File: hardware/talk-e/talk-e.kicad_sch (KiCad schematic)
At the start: 1 part, among them U1 RFM96W-433S2

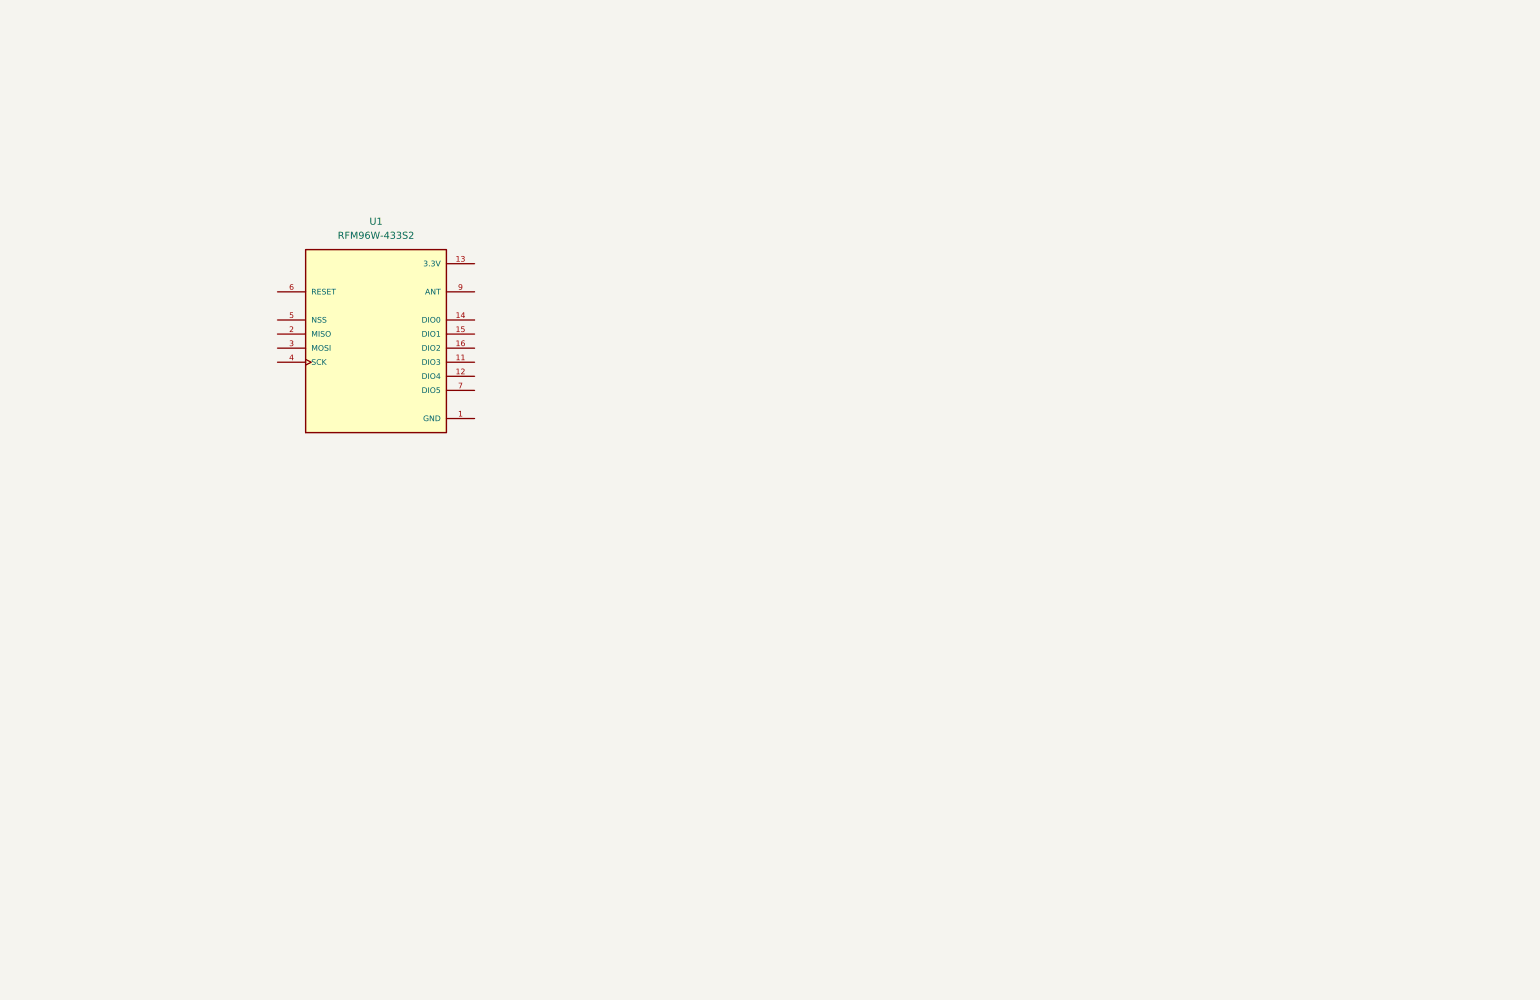
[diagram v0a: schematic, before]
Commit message: Progress on battery charging schematic
TP4056 + DW01A + FS8205A
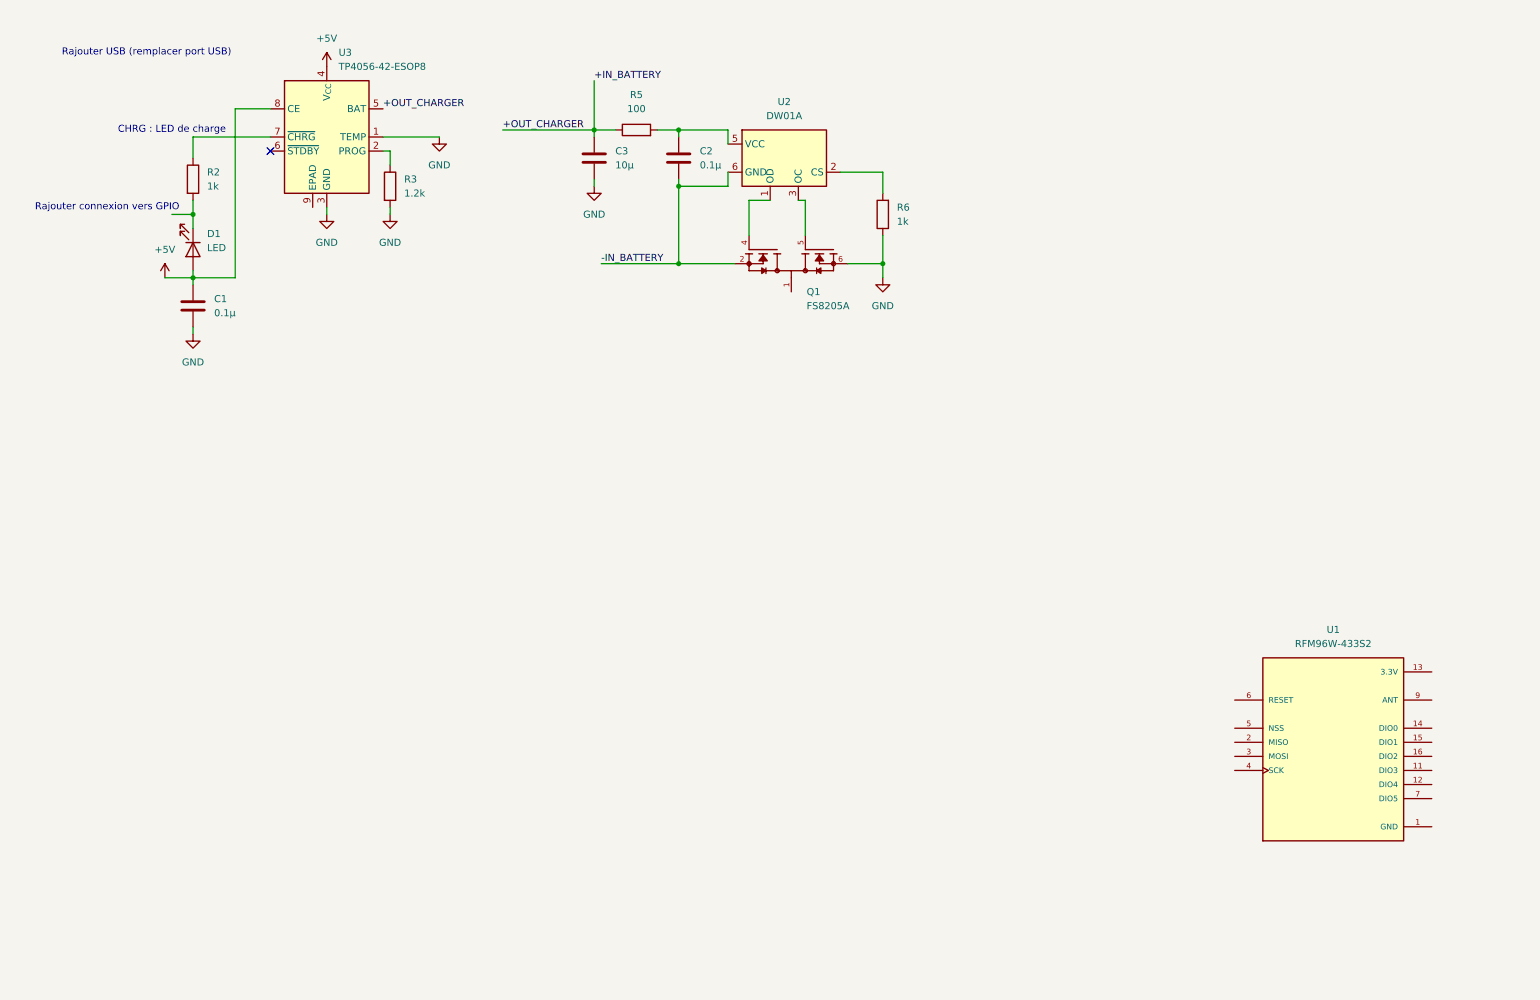
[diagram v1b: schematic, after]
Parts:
- added C1, C2: 0.1µ, symbol Device:C
- added C3: 10µ, symbol Device:C
- added D1: LED, LED_THT:LED_D3.0mm, symbol Device:LED
- added Q1: FS8205A, FS8205A:SOP65P640X120-8N, symbol FS8205A:FS8205A
- added R2, R6: 1k, symbol Device:R
- added R3: 1.2k, symbol Device:R
- added R5: 100, symbol Device:R
- added U2: DW01A, Package_TO_SOT_SMD:SOT-23-6, symbol Battery_Management:DW01A
- added U3: TP4056-42-ESOP8, Package_SO:SOIC-8-1EP_3.9x4.9mm_P1.27mm_EP2.41x3.3mm, symbol Battery_Management:TP4056-42-ESOP8
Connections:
- net GND: now also C1.2, C3.2, Q1.6, Q1.7, R3.2, R6.1, U3.1 (TEMP), U3.3 (GND)
- new net: D1.1 (K), R2.2
- new net: C2.1, R5.2, U2.5 (VCC)
- new net: R6.2, U2.2 (CS)
- new net: R3.1, U3.2 (PROG)
- new net: R2.1, U3.7 (~{CHRG})
- new net: Q1.4, U2.1 (OD)
- new net: Q1.5, U2.3 (OC)
- new net: Q1.1, Q1.8
- new net +5V: C1.1, D1.2 (A), U3.4 (V_{CC}), U3.8 (CE)
- new net +IN_BATTERY: C3.1, R5.1, U3.5 (BAT)
- new net -IN_BATTERY: C2.2, Q1.2, Q1.3, U2.6 (GND)
- no-connect marks 0 -> 1
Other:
- note added: "CHRG : LED de charge"
- note added: "Rajouter USB (remplacer port USB)"
- note added: "Rajouter connexion vers GPIO"
- moved on the sheet: U1

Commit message: Added SX1278 connections to ESP32-S3 in schematic
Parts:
- added U4: ESP32-S3, Package_DFN_QFN:QFN-56-1EP_7x7mm_P0.4mm_EP4x4mm, symbol MCU_Espressif:ESP32-S3
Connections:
- net GND: now also U4.57 (GND)
- net +3.3V: now reaches U1.13 (3.3V)
- net LORA_DIO0: now reaches U1.14 (DIO0)
- net LORA_DIO0: now also U4.14 (GPIO9)
- net LORA_MISO: now reaches U1.2 (MISO)
- net LORA_MISO: now also U4.18 (GPIO13)
- net LORA_MOSI: now reaches U1.3 (MOSI)
- net LORA_MOSI: now also U4.16 (GPIO11)
- net LORA_SCK: now reaches U1.4 (SCK)
- net LORA_SCK: now also U4.17 (GPIO12)
- net LORA_CS: now reaches U1.5 (NSS)
- net LORA_CS: now also U4.15 (GPIO10)
- net LORA_RST: now reaches U1.6 (RESET)
- net LORA_RST: now also U4.13 (GPIO8)
- net ANTENNA: now reaches U1.9 (ANT)
- new net: U4.2 (VDD3P3), U4.3 (VDD3P3)
- new net: U4.55 (VDDA), U4.56 (VDDA)
- no-connect marks 1 -> 6
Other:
- note added: "3.7 V nominal"
- note added: "Brancher la batterie sur IN_BATTERY"
- moved on the sheet: U1

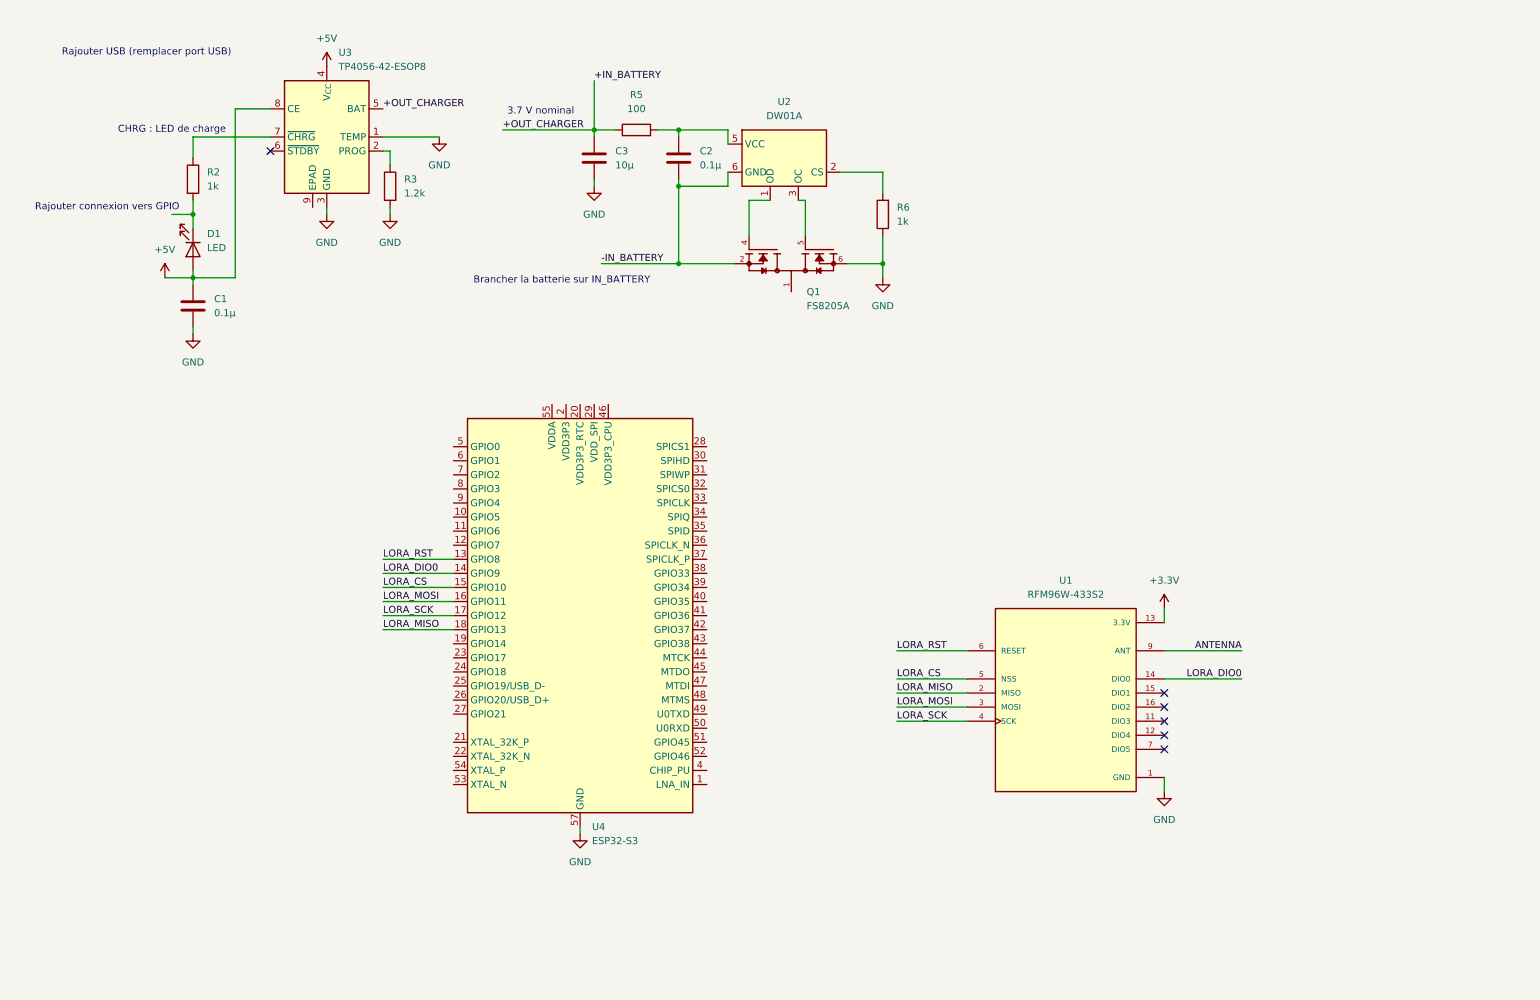
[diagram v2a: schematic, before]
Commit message: Added SH1106 OLED screen to schematic
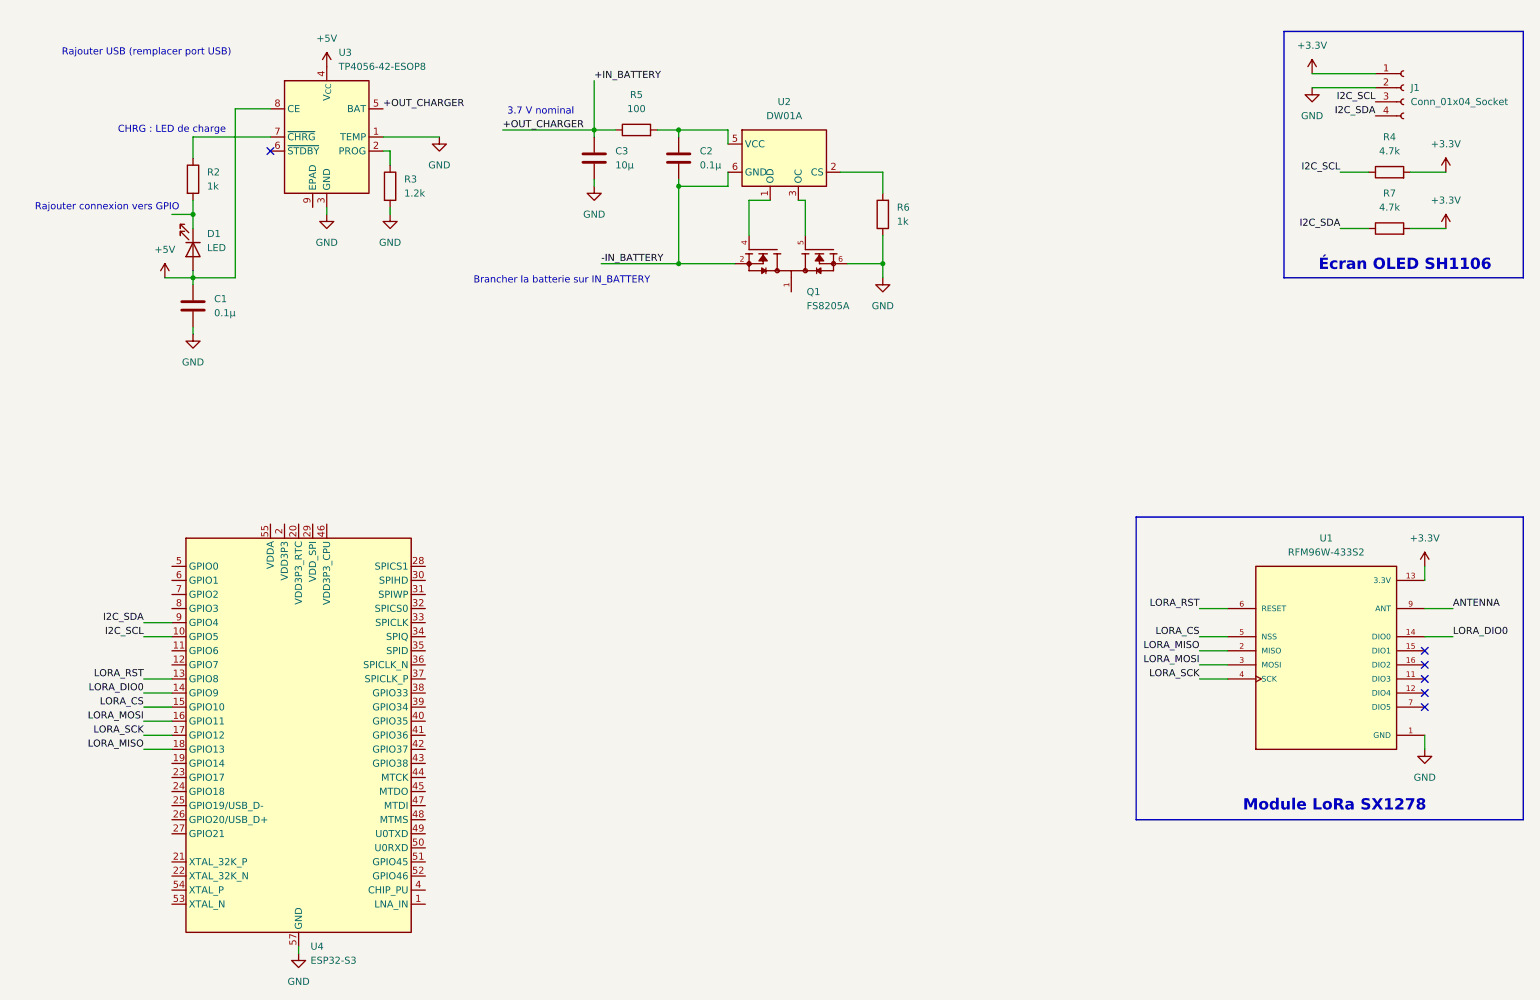
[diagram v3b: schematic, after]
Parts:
- added J1: Conn_01x04_Socket, Connector_PinSocket_2.54mm:PinSocket_1x04_P2.54mm_Vertical, symbol Connector:Conn_01x04_Socket
- added R4, R7: 4.7k, symbol Device:R
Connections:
- net +3.3V: now also J1.1 (Pin_1), R4.2, R7.2
- net GND: now also J1.2 (Pin_2)
- net I2C_SCL: now reaches U4.10 (GPIO5)
- net I2C_SCL: now also J1.3 (Pin_3), R4.1
- net I2C_SDA: now reaches U4.9 (GPIO4)
- net I2C_SDA: now also J1.4 (Pin_4), R7.1
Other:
- note added: "Module LoRa SX1278"
- note added: "Écran OLED SH1106"
- moved on the sheet: U1, U4

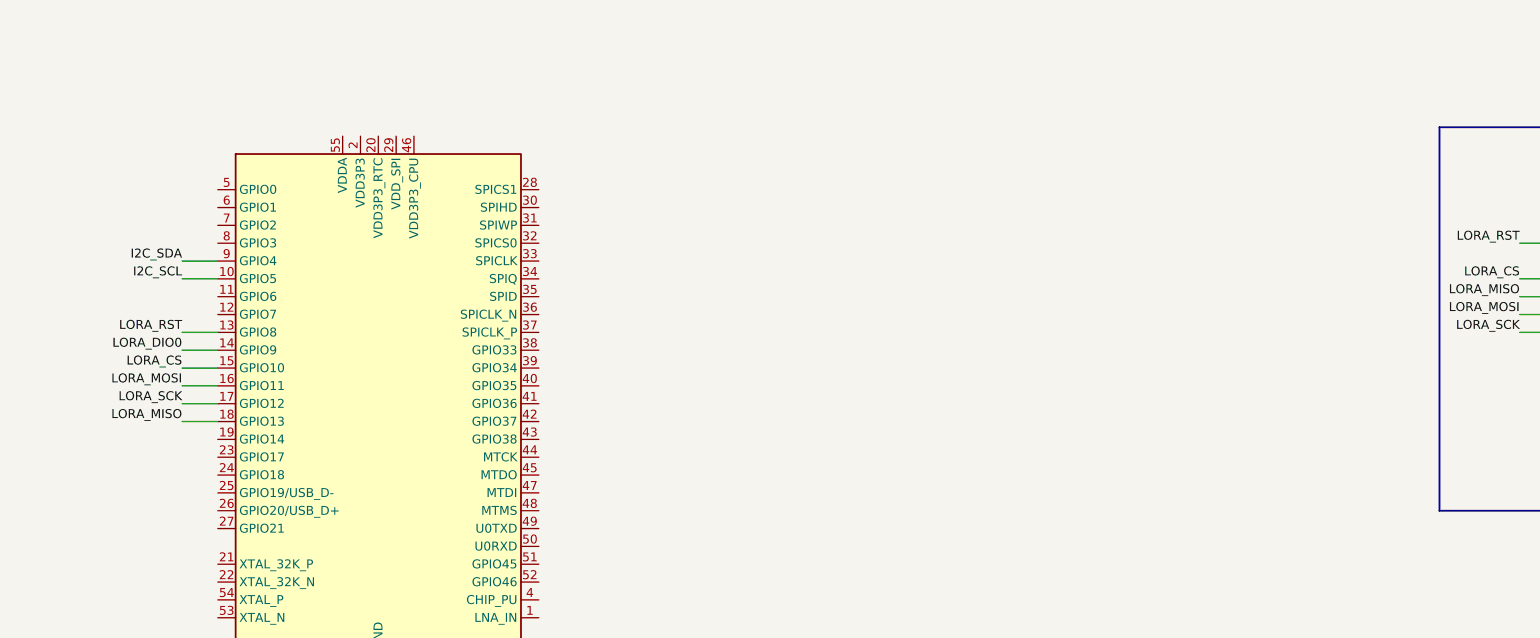
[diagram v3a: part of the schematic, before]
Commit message: Added EC12 incremental encoder to schematic
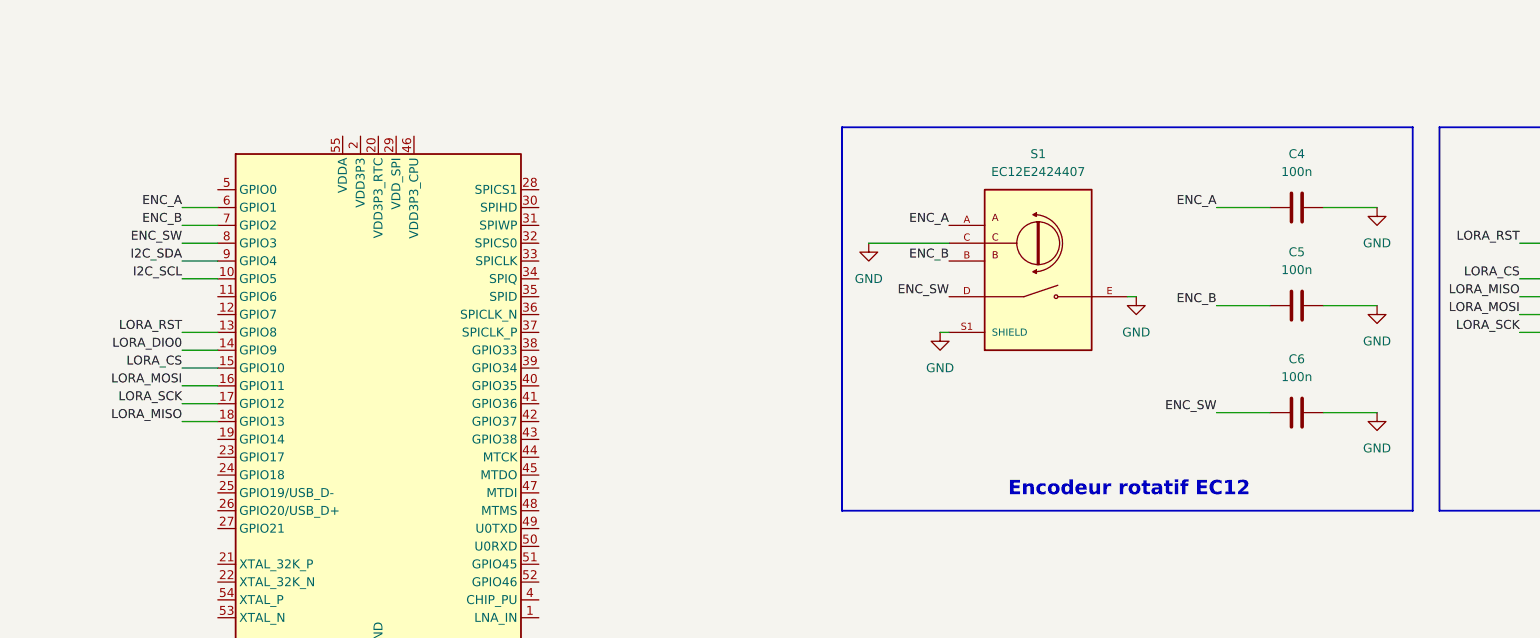
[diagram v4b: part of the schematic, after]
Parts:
- added C4, C5, C6: 100n, symbol Device:C
- added S1: EC12E2424407, EC12E2424407:ALPS_EC12E2424407, symbol EC12E2424407:EC12E2424407
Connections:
- net GND: now also C4.2, C5.2, C6.2, S1.C, S1.E, S1.S1 (SHIELD), S1.S2 (SHIELD)
- net ENC_A: now reaches U4.6 (GPIO1)
- net ENC_A: now also C4.1, S1.A
- net ENC_B: now reaches U4.7 (GPIO2)
- net ENC_B: now also C5.1, S1.B
- net ENC_SW: now reaches U4.8 (GPIO3)
- net ENC_SW: now also C6.1, S1.D
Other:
- note added: "Encodeur rotatif EC12"
